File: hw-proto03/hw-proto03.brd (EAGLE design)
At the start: 87.3 x 68.6 mm, 37 parts, among them IC1 TLV74333PDBVR, IC2 IR4427S, IC3 MCP2562T, IC5 IR4427S, J1 J15MM, J2 J5MM, J3 J12MM, J4 J5MM, Q1 SQJ147ELP-T1_GE3, Q2 SQJ147ELP-T1_GE3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

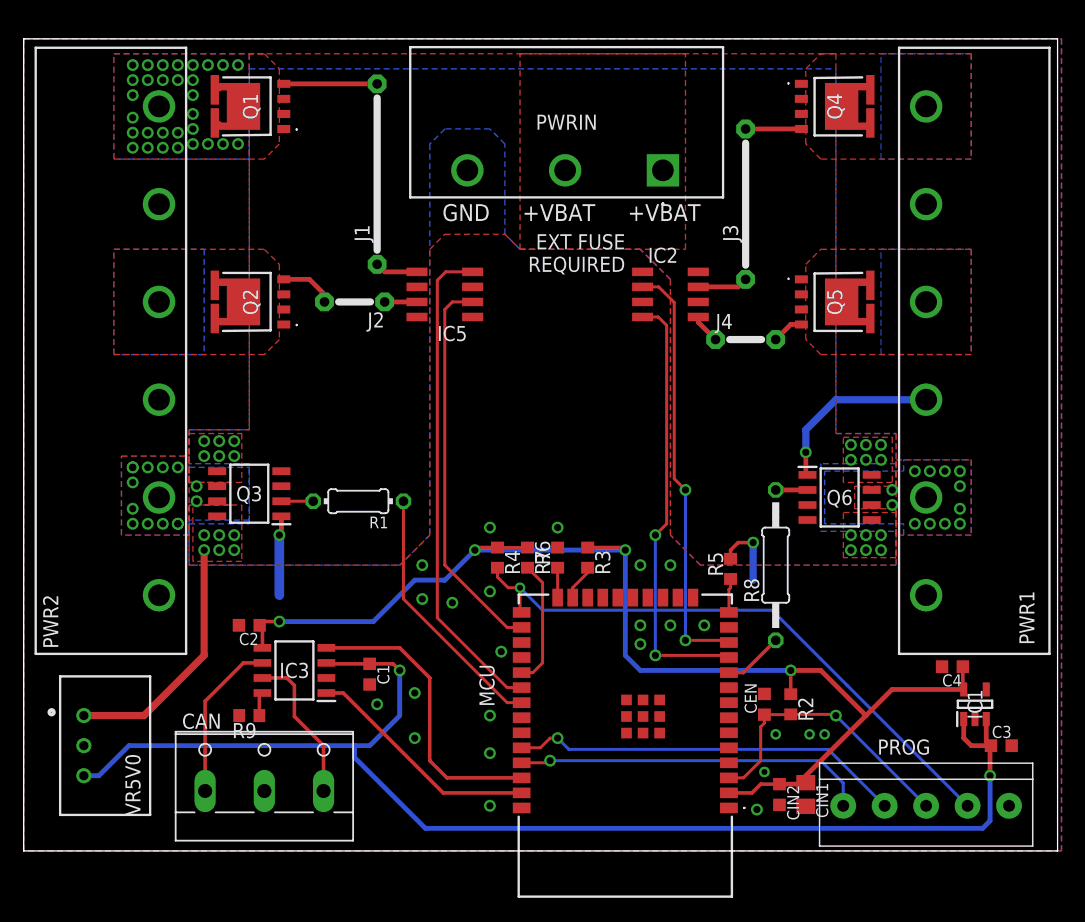
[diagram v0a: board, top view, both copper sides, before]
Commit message: layout refinement, added stiching
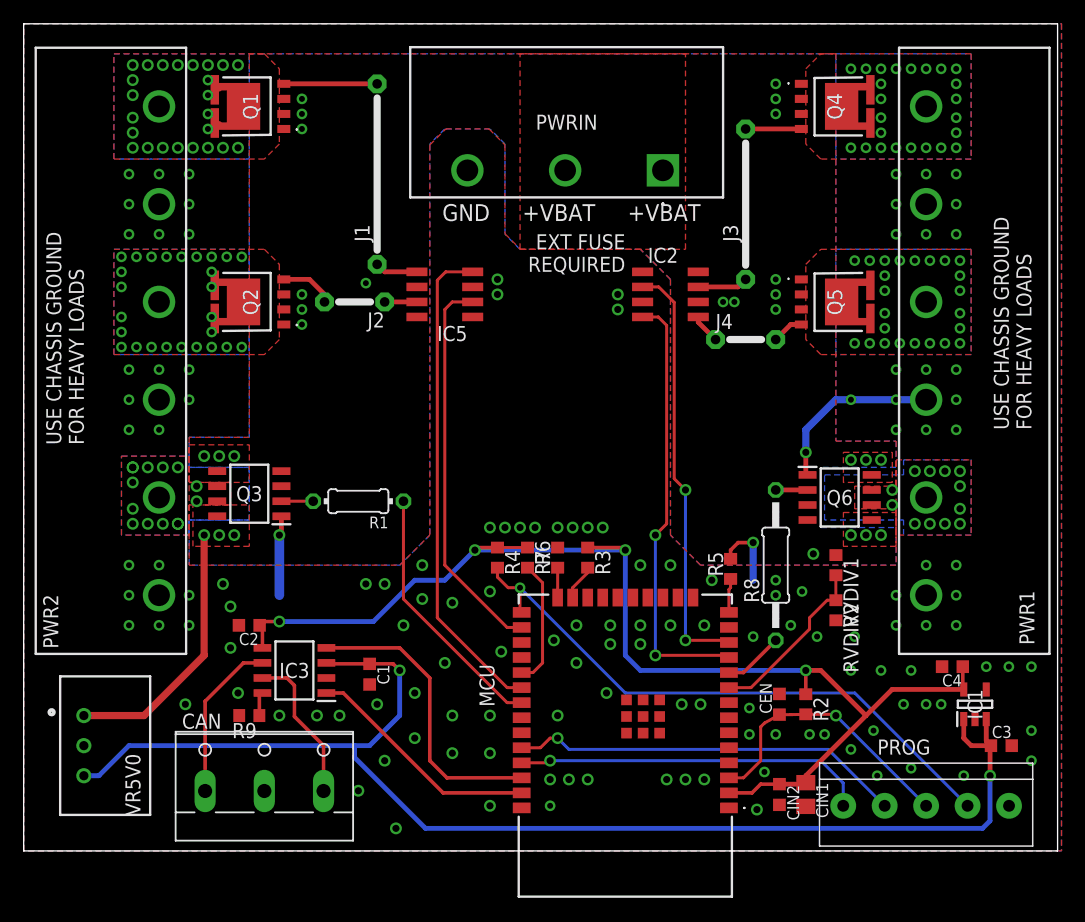
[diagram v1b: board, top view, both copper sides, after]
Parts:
- added RVDIV1: 33K0, rcl:R0603
- added RVDIV2: 8K2, rcl:R0603
- moved CEN 1.27 mm to (65.1, 13.7)
- moved R2 1.27 mm to (67.3, 13.7)
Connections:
- new net ADC1_0: MCU.4
- new net ADC1_3: MCU.5
- new net ADC1_5: MCU.9, RVDIV1.2, RVDIV2.1
- new net ADC1_6: MCU.6
- new net ADC1_7: MCU.7
- new net ADC2_6: MCU.13
- net +12V: now also RVDIV1.1
- net GND: now also RVDIV2.2
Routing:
- net ADC1_5: track 0.00 -> 14.8 mm
- net +12V: track 21.2 -> 22.4 mm, vias 24 -> 28
- net EN: track 24.1 -> 23.6 mm
- net SW1: vias 30 -> 24
- net GND: vias 27 -> 142
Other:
- board size 87.3 x 68.6 mm -> 87.3 x 69.8 mm
- board text added: "USE CHASSIS GROUND FOR HEAVY LOADS"

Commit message: added passives, refined layout
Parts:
- added CIN3, CIN5: 100n, rcl:C0603K
- added CIN4, CIN6: 4u7, rcl:C0805K
- J1: value J15MM -> J12MM; device jumper:15 -> jumper:12
- J4: value J5MM -> J7MM; device jumper:05 -> jumper:07
- moved J3 2.54 mm to (62.2, 58.4)
- moved J1 1.80 mm to (32.4, 59.7)
- moved J4 0.71 mm to (61.9, 43.8)
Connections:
- net +12V: now also CIN3.1, CIN4.1, CIN5.1, CIN6.1
- net GND: now also CIN3.2, CIN4.2, CIN5.2, CIN6.2
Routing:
- net GND: track 27.9 -> 53.3 mm, vias 142 -> 144
- net N$9: track 4.26 -> 6.06 mm
- net N$10: track 4.71 -> 6.50 mm
- net N$5: track 7.88 -> 9.15 mm
- net N$4: track 3.63 -> 4.41 mm
- net +12V: vias 28 -> 44
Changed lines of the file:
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@@
 </element>
 <element name="R8" library="rcl" package="0207/12" value="10K0" x="64.77" y="25.4" rot="R90"/>
-<element name="J1" library="jumper" package="15" value="J15MM" x="31.115" y="58.42" rot="R90"/>
+<element name="J1" library="jumper" package="12" value="J12MM" x="32.385" y="59.69" rot="R90"/>
 <element name="J2" library="jumper" package="05" value="J5MM" x="29.21" y="47.625" rot="R180"/>
-<element name="J3" library="jumper" package="12" value="J12MM" x="62.23" y="55.88" rot="R90"/>
-<element name="J4" library="jumper" package="05" value="J5MM" x="62.23" y="44.45"/>
+<element name="J3" library="jumper" package="12" value="J12MM" x="62.23" y="58.42" rot="R90"/>
+<element name="J4" library="jumper" package="07" value="J7MM" x="61.9125" y="43.815"/>
 <element name="IC1" library="TLV74333PDBVR" package="SOT95P280X145-5N" value="TLV74333PDBVR" x="81.5975" y="13.6525" rot="R90">
 <attribute name="DESCRIPTION" value="300mA Low-Dropout (LDO) Regulator" x="81.5975" y="13.6525" size="1.27" layer="27" font="vector" ratio="14" rot="R90" display="off"/>
@@
 <element name="RVDIV1" library="rcl" package="R0603" value="33K0" x="69.85" y="25.4" rot="R270"/>
 <element name="RVDIV2" library="rcl" package="R0603" value="8K2" x="69.85" y="21.59" rot="R270"/>
+<element name="CIN3" library="rcl" package="C0603K" value="100n" x="31.4325" y="50.4825" rot="R90"/>
+<element name="CIN4" library="rcl" package="C0805K" value="4u7" x="28.8925" y="51.435" rot="R90"/>
+<element name="CIN5" library="rcl" package="C0603K" value="100n" x="60.6425" y="46.6725" rot="R270"/>
+<element name="CIN6" library="rcl" package="C0805K" value="4u7" x="63.1825" y="46.99" rot="R270"/>
 </elements>
 <signals>
@@
 <via x="48.895" y="28.575" extent="1-16" drill="0.6"/>
 <via x="50.165" y="28.575" extent="1-16" drill="0.6"/>
-<via x="41.275" y="49.53" extent="1-16" drill="0.6"/>
-<via x="41.275" y="48.26" extent="1-16" drill="0.6"/>
-<via x="51.435" y="48.26" extent="1-16" drill="0.6"/>
-<via x="51.435" y="46.99" extent="1-16" drill="0.6"/>
 <via x="59.3725" y="24.13" extent="1-16" drill="0.6"/>
 <via x="50.8" y="20.32" extent="1-16" drill="0.6"/>
@@
 <via x="74.93" y="36.83" extent="1-16" drill="0.5"/>
 <via x="66.04" y="20.32" extent="1-16" drill="0.5"/>
+<contactref element="CIN4" pad="2"/>
+<contactref element="CIN3" pad="2"/>
+<contactref element="CIN5" pad="2"/>
+<contactref element="CIN6" pad="2"/>
+<via x="60.6425" y="43.4975" extent="1-16" drill="0.6" shape="octagon"/>
+<wire x1="63.1825" y1="45.99" x2="60.835" y2="45.99" width="0.4064" layer="1"/>
+<wire x1="60.835" y1="45.99" x2="60.6425" y2="45.7975" width="0.4064" layer="1"/>
+<via x="51.435" y="48.26" extent="1-16" drill="0.6"/>
+<via x="51.435" y="46.99" extent="1-16" drill="0.6"/>
+<via x="41.275" y="49.53" extent="1-16" drill="0.6"/>
+<via x="41.275" y="48.26" extent="1-16" drill="0.6"/>
+<wire x1="60.6425" y1="43.4975" x2="60.6425" y2="42.8625" width="0.6096" layer="16"/>
+<wire x1="60.6425" y1="42.8625" x2="59.69" y2="41.91" width="0.6096" layer="16"/>
+<wire x1="59.69" y1="41.91" x2="54.61" y2="41.91" width="0.6096" layer="16"/>
+<wire x1="60.6425" y1="45.7975" x2="60.6425" y2="43.4975" width="0.4064" layer="1"/>
+<via x="29.21" y="54.61" extent="1-16" drill="0.6" shape="octagon"/>
+<wire x1="29.21" y1="54.61" x2="30.48" y2="55.88" width="0.6096" layer="16"/>
+<wire x1="30.48" y1="55.88" x2="36.83" y2="55.88" width="0.6096" layer="16"/>
+<wire x1="28.8925" y1="52.435" x2="28.8925" y2="54.2925" width="0.4064" layer="1"/>
+<wire x1="28.8925" y1="54.2925" x2="29.21" y2="54.61" width="0.4064" layer="1"/>
+<wire x1="31.4325" y1="51.3575" x2="30.355" y2="52.435" width="0.4064" layer="1"/>
+<wire x1="30.355" y1="52.435" x2="28.8925" y2="52.435" width="0.4064" layer="1"/>
 </signal>
 <signal name="SW1">
@@
 <via x="64.77" y="46.99" extent="1-16" drill="0.5"/>
 <wire x1="16.51" y1="17.78" x2="16.51" y2="27.94" width="0.6096" layer="1"/>
-<via x="30.1625" y="49.2125" extent="1-16" drill="0.5"/>
-<via x="60.325" y="47.625" extent="1-16" drill="0.5"/>
-<via x="61.2775" y="47.625" extent="1-16" drill="0.5"/>
 <contactref element="RVDIV1" pad="1"/>
 <via x="67.945" y="26.3525" extent="1-16" drill="0.6"/>
+<contactref element="CIN4" pad="1"/>
+<contactref element="CIN3" pad="1"/>
+<contactref element="CIN6" pad="1"/>
+<contactref element="CIN5" pad="1"/>
+<via x="64.77" y="41.91" extent="1-16" drill="0.5"/>
+<via x="66.04" y="41.91" extent="1-16" drill="0.5"/>
+<via x="67.31" y="41.91" extent="1-16" drill="0.5"/>
+<via x="68.58" y="41.91" extent="1-16" drill="0.5"/>
+<via x="69.215" y="36.83" extent="1-16" drill="0.5"/>
+<via x="69.85" y="34.29" extent="1-16" drill="0.5"/>
+<via x="68.58" y="36.195" extent="1-16" drill="0.5"/>
+<via x="68.58" y="34.6075" extent="1-16" drill="0.5"/>
+<via x="31.115" y="59.055" extent="1-16" drill="0.6"/>
+<via x="29.845" y="59.055" extent="1-16" drill="0.6"/>
+<via x="29.845" y="57.785" extent="1-16" drill="0.6"/>
+<via x="33.02" y="57.785" extent="1-16" drill="0.6"/>
+<via x="33.02" y="59.055" extent="1-16" drill="0.6"/>
+<via x="34.925" y="54.61" extent="1-16" drill="0.6"/>
+<via x="29.845" y="48.5775" extent="1-16" drill="0.6"/>
+<via x="28.575" y="48.5775" extent="1-16" drill="0.6"/>
+<via x="34.6075" y="44.7675" extent="1-16" drill="0.6"/>
+<via x="33.02" y="44.7675" extent="1-16" drill="0.6"/>
+<via x="31.4325" y="44.7675" extent="1-16" drill="0.6"/>
 </signal>
 <signal name="+5V">
@@
 <contactref element="IC5" pad="5"/>
 <contactref element="J1" pad="1"/>
-<wire x1="34.48" y1="50.165" x2="31.75" y2="50.165" width="0.4064" layer="1"/>
-<wire x1="31.75" y1="50.165" x2="31.115" y2="50.8" width="0.4064" layer="1"/>
+<wire x1="32.385" y1="53.34" x2="33.02" y2="53.34" width="0.6096" layer="1"/>
+<wire x1="33.02" y1="53.34" x2="34.29" y2="52.07" width="0.6096" layer="1"/>
+<wire x1="34.29" y1="52.07" x2="34.29" y2="50.355" width="0.6096" layer="1"/>
+<wire x1="34.29" y1="50.355" x2="34.48" y2="50.165" width="0.6096" layer="1"/>
 </signal>
 <signal name="CTL2">
@@
 <contactref element="Q1" pad="4"/>
 <contactref element="J1" pad="2"/>
-<wire x1="23.233" y1="66.04" x2="31.115" y2="66.04" width="0.4064" layer="1"/>
+<wire x1="23.233" y1="66.04" x2="32.385" y2="66.04" width="0.6096" layer="1"/>
 </signal>
 <signal name="N$6">
 <contactref element="Q2" pad="4"/>
 <contactref element="J2" pad="2"/>
-<wire x1="26.67" y1="47.625" x2="26.67" y2="48.26" width="0.4064" layer="1"/>
-<wire x1="26.67" y1="48.26" x2="25.4" y2="49.53" width="0.4064" layer="1"/>
-<wire x1="25.4" y1="49.53" x2="23.233" y2="49.53" width="0.4064" layer="1"/>
+<wire x1="26.67" y1="47.625" x2="26.67" y2="48.26" width="0.6096" layer="1"/>
+<wire x1="26.67" y1="48.26" x2="25.4" y2="49.53" width="0.6096" layer="1"/>
+<wire x1="25.4" y1="49.53" x2="23.233" y2="49.53" width="0.6096" layer="1"/>
 </signal>
 <signal name="N$7">
@@
 <contactref element="IC2" pad="5"/>
 <contactref element="J4" pad="1"/>
-<wire x1="58.23" y1="46.355" x2="58.23" y2="45.91" width="0.4064" layer="1"/>
-<wire x1="58.23" y1="45.91" x2="59.69" y2="44.45" width="0.4064" layer="1"/>
+<wire x1="58.23" y1="46.355" x2="58.23" y2="43.9425" width="0.6096" layer="1"/>
+<wire x1="58.23" y1="43.9425" x2="58.1025" y2="43.815" width="0.6096" layer="1"/>
 </signal>
 <signal name="N$9">
 <contactref element="IC2" pad="7"/>
 <contactref element="J3" pad="1"/>
-<wire x1="58.23" y1="48.895" x2="61.595" y2="48.895" width="0.4064" layer="1"/>
-<wire x1="61.595" y1="48.895" x2="62.23" y2="49.53" width="0.4064" layer="1"/>
+<wire x1="58.23" y1="48.895" x2="60.325" y2="48.895" width="0.6096" layer="1"/>
+<wire x1="60.325" y1="48.895" x2="62.23" y2="50.8" width="0.6096" layer="1"/>
+<wire x1="62.23" y1="52.07" x2="62.23" y2="50.8" width="0.6096" layer="1"/>
 </signal>
 <signal name="N$10">
 <contactref element="Q4" pad="4"/>
 <contactref element="J3" pad="2"/>
-<wire x1="66.937" y1="62.23" x2="62.23" y2="62.23" width="0.4064" layer="1"/>
+<wire x1="66.937" y1="62.23" x2="63.5" y2="62.23" width="0.6096" layer="1"/>
+<wire x1="63.5" y1="62.23" x2="62.23" y2="63.5" width="0.6096" layer="1"/>
+<wire x1="62.23" y1="63.5" x2="62.23" y2="64.77" width="0.6096" layer="1"/>
 </signal>
 <signal name="N$11">
 <contactref element="Q5" pad="4"/>
 <contactref element="J4" pad="2"/>
-<wire x1="66.937" y1="45.72" x2="66.04" y2="45.72" width="0.4064" layer="1"/>
-<wire x1="66.04" y1="45.72" x2="64.77" y2="44.45" width="0.4064" layer="1"/>
+<wire x1="66.937" y1="45.72" x2="66.937" y2="45.0295" width="0.6096" layer="1"/>
+<wire x1="66.937" y1="45.0295" x2="65.7225" y2="43.815" width="0.6096" layer="1"/>
 </signal>
 <signal name="SW4">
@@
 <contactref element="IC5" pad="7"/>
 <contactref element="J2" pad="1"/>
-<wire x1="34.48" y1="47.625" x2="31.75" y2="47.625" width="0.4064" layer="1"/>
+<wire x1="34.48" y1="47.625" x2="31.75" y2="47.625" width="0.6096" layer="1"/>
 </signal>
 <signal name="CANSTBY">
